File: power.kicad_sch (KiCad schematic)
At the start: 13 parts, among them J1 Conn_01x04, J2 Conn_01x04

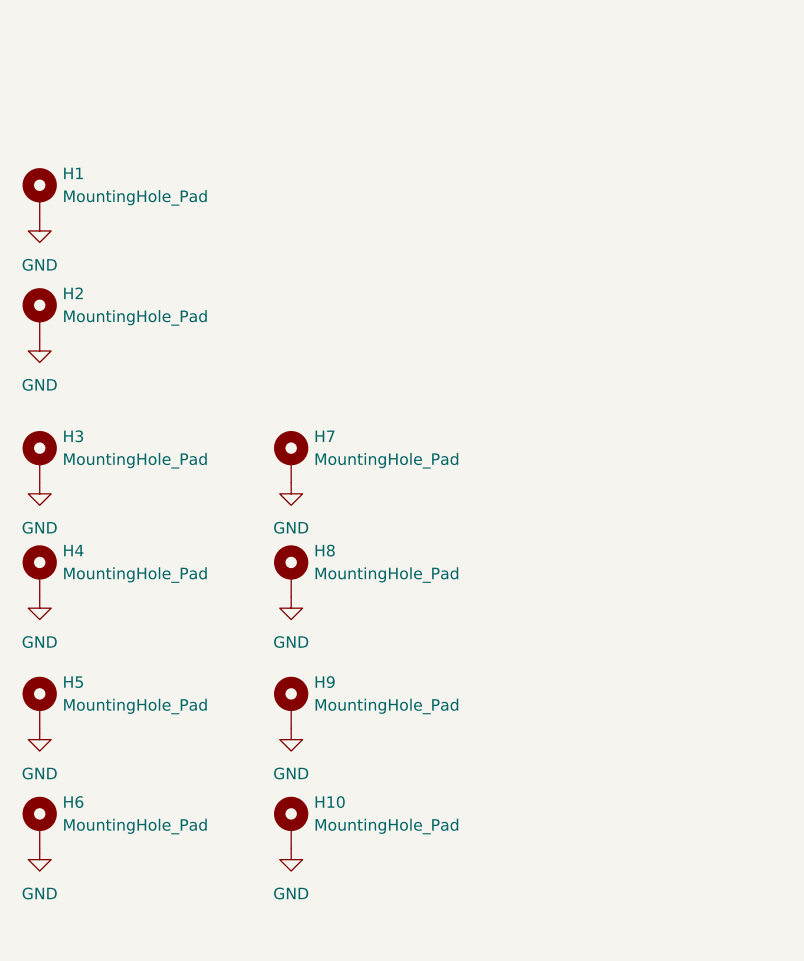
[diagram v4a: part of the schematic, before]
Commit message: correct hole positions
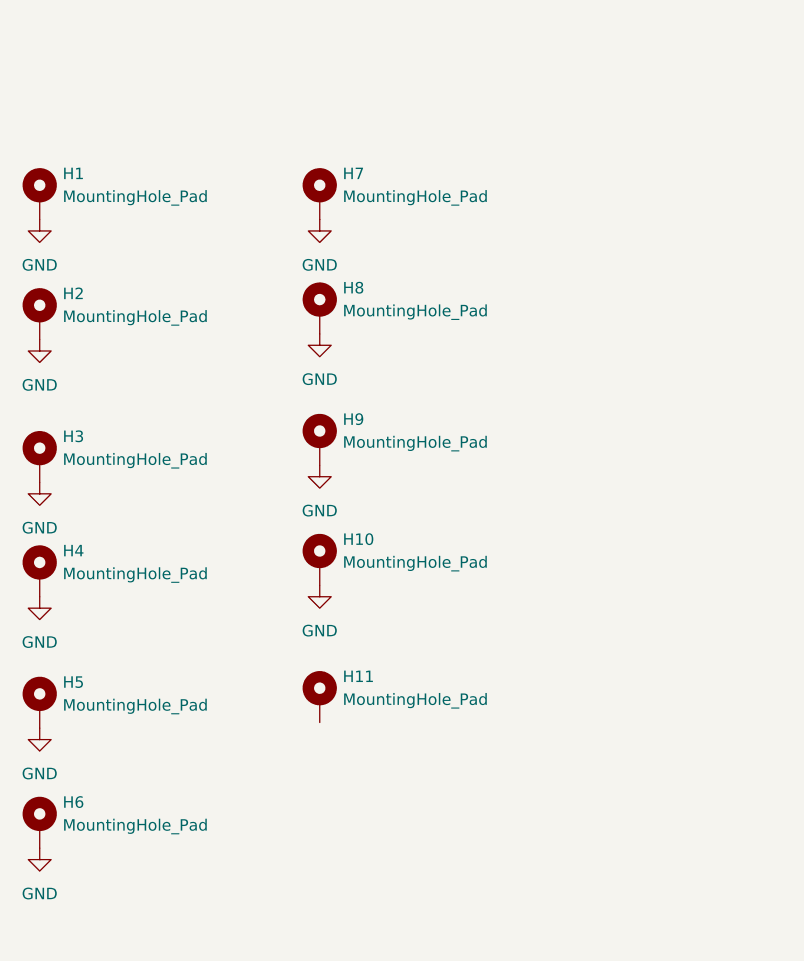
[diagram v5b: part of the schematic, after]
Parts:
- added H11: MountingHole_Pad, MountingHole:MountingHole_3.2mm_M3_DIN965_Pad, symbol Mechanical:MountingHole_Pad
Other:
- moved on the sheet: H10, H7, H8, H9
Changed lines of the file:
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@@
     )
   )
-  (symbol (lib_id "power:GND") (at 47.625 143.51 0) (unit 1)
-    (in_bom yes) (on_board yes) (fields_autoplaced)
-    (property "Reference" "#PWR07" (id 0) (at 47.625 149.86 0)
-      (effects (font (size 1.27 1.27)) hide)
-    )
-    (property "Value" "GND" (id 1) (at 47.625 148.59 0))
-    (property "Footprint" "" (id 2) (at 47.625 143.51 0)
-      (effects (font (size 1.27 1.27)) hide)
-    )
-    (property "Datasheet" "" (id 3) (at 47.625 143.51 0)
+  (symbol (lib_id "power:GND") (at 50.8 114.3 0) (unit 1)
+    (in_bom yes) (on_board yes) (fields_autoplaced)
+    (property "Reference" "#PWR07" (id 0) (at 50.8 120.65 0)
+      (effects (font (size 1.27 1.27)) hide)
+    )
+    (property "Value" "GND" (id 1) (at 50.8 119.38 0))
+    (property "Footprint" "" (id 2) (at 50.8 114.3 0)
+      (effects (font (size 1.27 1.27)) hide)
+    )
+    (property "Datasheet" "" (id 3) (at 50.8 114.3 0)
       (effects (font (size 1.27 1.27)) hide)
     )
@@
     (pin "1")
   )
-  (symbol (lib_id "Mechanical:MountingHole_Pad") (at 47.625 181.61 0) (unit 1)
-    (in_bom yes) (on_board yes) (fields_autoplaced)
-    (property "Reference" "H10" (id 0) (at 50.165 179.0699 0)
-      (effects (font (size 1.27 1.27)) (justify left))
-    )
-    (property "Value" "MountingHole_Pad" (id 1) (at 50.165 181.6099 0)
-      (effects (font (size 1.27 1.27)) (justify left))
-    )
-    (property "Footprint" "MountingHole:MountingHole_3.2mm_M3_DIN965_Pad" (id 2) (at 47.625 181.61 0)
-      (effects (font (size 1.27 1.27)) hide)
-    )
-    (property "Datasheet" "~" (id 3) (at 47.625 181.61 0)
+  (symbol (lib_id "Mechanical:MountingHole_Pad") (at 50.8 152.4 0) (unit 1)
+    (in_bom yes) (on_board yes)
+    (property "Reference" "H10" (id 0) (at 53.34 149.8599 0)
+      (effects (font (size 1.27 1.27)) (justify left))
+    )
+    (property "Value" "MountingHole_Pad" (id 1) (at 53.34 152.3999 0)
+      (effects (font (size 1.27 1.27)) (justify left))
+    )
+    (property "Footprint" "MountingHole:MountingHole_3.2mm_M3_DIN965_Pad" (id 2) (at 50.8 152.4 0)
+      (effects (font (size 1.27 1.27)) hide)
+    )
+    (property "Datasheet" "~" (id 3) (at 50.8 152.4 0)
       (effects (font (size 1.27 1.27)) hide)
     )
@@
     )
   )
-  (symbol (lib_id "Mechanical:MountingHole_Pad") (at 47.625 168.275 0) (unit 1)
-    (in_bom yes) (on_board yes) (fields_autoplaced)
-    (property "Reference" "H9" (id 0) (at 50.165 165.7349 0)
-      (effects (font (size 1.27 1.27)) (justify left))
-    )
-    (property "Value" "MountingHole_Pad" (id 1) (at 50.165 168.2749 0)
-      (effects (font (size 1.27 1.27)) (justify left))
-    )
-    (property "Footprint" "MountingHole:MountingHole_3.2mm_M3_DIN965_Pad" (id 2) (at 47.625 168.275 0)
-      (effects (font (size 1.27 1.27)) hide)
-    )
-    (property "Datasheet" "~" (id 3) (at 47.625 168.275 0)
+  (symbol (lib_id "Mechanical:MountingHole_Pad") (at 50.8 139.065 0) (unit 1)
+    (in_bom yes) (on_board yes)
+    (property "Reference" "H9" (id 0) (at 53.34 136.5249 0)
+      (effects (font (size 1.27 1.27)) (justify left))
+    )
+    (property "Value" "MountingHole_Pad" (id 1) (at 53.34 139.0649 0)
+      (effects (font (size 1.27 1.27)) (justify left))
+    )
+    (property "Footprint" "MountingHole:MountingHole_3.2mm_M3_DIN965_Pad" (id 2) (at 50.8 139.065 0)
+      (effects (font (size 1.27 1.27)) hide)
+    )
+    (property "Datasheet" "~" (id 3) (at 50.8 139.065 0)
       (effects (font (size 1.27 1.27)) hide)
     )
@@
     (pin "1")
   )
-  (symbol (lib_id "Mechanical:MountingHole_Pad") (at 47.625 153.67 0) (unit 1)
-    (in_bom yes) (on_board yes) (fields_autoplaced)
-    (property "Reference" "H8" (id 0) (at 50.165 151.1299 0)
-      (effects (font (size 1.27 1.27)) (justify left))
-    )
-    (property "Value" "MountingHole_Pad" (id 1) (at 50.165 153.6699 0)
-      (effects (font (size 1.27 1.27)) (justify left))
-    )
-    (property "Footprint" "MountingHole:MountingHole_3.2mm_M3_DIN965_Pad" (id 2) (at 47.625 153.67 0)
-      (effects (font (size 1.27 1.27)) hide)
-    )
-    (property "Datasheet" "~" (id 3) (at 47.625 153.67 0)
-      (effects (font (size 1.27 1.27)) hide)
-    )
-    (pin "1")
-  )
-  (symbol (lib_id "power:GND") (at 47.625 156.21 0) (unit 1)
-    (in_bom yes) (on_board yes) (fields_autoplaced)
-    (property "Reference" "#PWR08" (id 0) (at 47.625 162.56 0)
-      (effects (font (size 1.27 1.27)) hide)
-    )
-    (property "Value" "GND" (id 1) (at 47.625 161.29 0))
-    (property "Footprint" "" (id 2) (at 47.625 156.21 0)
-      (effects (font (size 1.27 1.27)) hide)
-    )
-    (property "Datasheet" "" (id 3) (at 47.625 156.21 0)
-      (effects (font (size 1.27 1.27)) hide)
-    )
-    (pin "1")
-  )
-  (symbol (lib_id "power:GND") (at 47.625 170.815 0) (unit 1)
-    (in_bom yes) (on_board yes) (fields_autoplaced)
-    (property "Reference" "#PWR09" (id 0) (at 47.625 177.165 0)
-      (effects (font (size 1.27 1.27)) hide)
-    )
-    (property "Value" "GND" (id 1) (at 47.625 175.895 0))
-    (property "Footprint" "" (id 2) (at 47.625 170.815 0)
-      (effects (font (size 1.27 1.27)) hide)
-    )
-    (property "Datasheet" "" (id 3) (at 47.625 170.815 0)
+  (symbol (lib_id "Mechanical:MountingHole_Pad") (at 50.8 124.46 0) (unit 1)
+    (in_bom yes) (on_board yes)
+    (property "Reference" "H8" (id 0) (at 53.34 121.9199 0)
+      (effects (font (size 1.27 1.27)) (justify left))
+    )
+    (property "Value" "MountingHole_Pad" (id 1) (at 53.34 124.4599 0)
+      (effects (font (size 1.27 1.27)) (justify left))
+    )
+    (property "Footprint" "MountingHole:MountingHole_3.2mm_M3_DIN965_Pad" (id 2) (at 50.8 124.46 0)
+      (effects (font (size 1.27 1.27)) hide)
+    )
+    (property "Datasheet" "~" (id 3) (at 50.8 124.46 0)
+      (effects (font (size 1.27 1.27)) hide)
+    )
+    (pin "1")
+  )
+  (symbol (lib_id "power:GND") (at 50.8 127 0) (unit 1)
+    (in_bom yes) (on_board yes) (fields_autoplaced)
+    (property "Reference" "#PWR08" (id 0) (at 50.8 133.35 0)
+      (effects (font (size 1.27 1.27)) hide)
+    )
+    (property "Value" "GND" (id 1) (at 50.8 132.08 0))
+    (property "Footprint" "" (id 2) (at 50.8 127 0)
+      (effects (font (size 1.27 1.27)) hide)
+    )
+    (property "Datasheet" "" (id 3) (at 50.8 127 0)
+      (effects (font (size 1.27 1.27)) hide)
+    )
+    (pin "1")
+  )
+  (symbol (lib_id "power:GND") (at 50.8 141.605 0) (unit 1)
+    (in_bom yes) (on_board yes) (fields_autoplaced)
+    (property "Reference" "#PWR09" (id 0) (at 50.8 147.955 0)
+      (effects (font (size 1.27 1.27)) hide)
+    )
+    (property "Value" "GND" (id 1) (at 50.8 146.685 0))
+    (property "Footprint" "" (id 2) (at 50.8 141.605 0)
+      (effects (font (size 1.27 1.27)) hide)
+    )
+    (property "Datasheet" "" (id 3) (at 50.8 141.605 0)
       (effects (font (size 1.27 1.27)) hide)
     )
@@
     (pin "1")
   )
-  (symbol (lib_id "power:GND") (at 47.625 184.15 0) (unit 1)
-    (in_bom yes) (on_board yes) (fields_autoplaced)
-    (property "Reference" "#PWR010" (id 0) (at 47.625 190.5 0)
-      (effects (font (size 1.27 1.27)) hide)
-    )
-    (property "Value" "GND" (id 1) (at 47.625 189.23 0))
-    (property "Footprint" "" (id 2) (at 47.625 184.15 0)
-      (effects (font (size 1.27 1.27)) hide)
-    )
-    (property "Datasheet" "" (id 3) (at 47.625 184.15 0)
+  (symbol (lib_id "power:GND") (at 50.8 154.94 0) (unit 1)
+    (in_bom yes) (on_board yes) (fields_autoplaced)
+    (property "Reference" "#PWR010" (id 0) (at 50.8 161.29 0)
+      (effects (font (size 1.27 1.27)) hide)
+    )
+    (property "Value" "GND" (id 1) (at 50.8 160.02 0))
+    (property "Footprint" "" (id 2) (at 50.8 154.94 0)
+      (effects (font (size 1.27 1.27)) hide)
+    )
+    (property "Datasheet" "" (id 3) (at 50.8 154.94 0)
       (effects (font (size 1.27 1.27)) hide)
     )
@@
     (pin "1")
   )
+  (symbol (lib_id "Mechanical:MountingHole_Pad") (at 50.8 167.64 0) (unit 1)
+    (in_bom yes) (on_board yes)
+    (property "Reference" "H11" (id 0) (at 53.34 165.0999 0)
+      (effects (font (size 1.27 1.27)) (justify left))
+    )
+    (property "Value" "MountingHole_Pad" (id 1) (at 53.34 167.6399 0)
+      (effects (font (size 1.27 1.27)) (justify left))
+    )
+    (property "Footprint" "MountingHole:MountingHole_3.2mm_M3_DIN965_Pad" (id 2) (at 50.8 167.64 0)
+      (effects (font (size 1.27 1.27)) hide)
+    )
+    (property "Datasheet" "~" (id 3) (at 50.8 167.64 0)
+      (effects (font (size 1.27 1.27)) hide)
+    )
+    (pin "1")
+  )
   (symbol (lib_id "power:+5V") (at 133.35 86.36 0) (unit 1)
     (in_bom yes) (on_board yes) (fields_autoplaced)
@@
     (pin "1")
   )
-  (symbol (lib_id "Mechanical:MountingHole_Pad") (at 47.625 140.97 0) (unit 1)
-    (in_bom yes) (on_board yes) (fields_autoplaced)
-    (property "Reference" "H7" (id 0) (at 50.165 138.4299 0)
-      (effects (font (size 1.27 1.27)) (justify left))
-    )
-    (property "Value" "MountingHole_Pad" (id 1) (at 50.165 140.9699 0)
-      (effects (font (size 1.27 1.27)) (justify left))
-    )
-    (property "Footprint" "MountingHole:MountingHole_3.2mm_M3_DIN965_Pad" (id 2) (at 47.625 140.97 0)
-      (effects (font (size 1.27 1.27)) hide)
-    )
-    (property "Datasheet" "~" (id 3) (at 47.625 140.97 0)
-      (effects (font (size 1.27 1.27)) hide)
-    )
+  (symbol (lib_id "Mechanical:MountingHole_Pad") (at 50.8 111.76 0) (unit 1)
+    (in_bom yes) (on_board yes)
+    (property "Reference" "H7" (id 0) (at 53.34 109.2199 0)
+      (effects (font (size 1.27 1.27)) (justify left))
+    )
+    (property "Value" "MountingHole_Pad" (id 1) (at 53.34 111.7599 0)
+      (effects (font (size 1.27 1.27)) (justify left))
+    )
+    (property "Footprint" "MountingHole:MountingHole_3.2mm_M3_DIN965_Pad" (id 2) (at 50.8 111.76 0)
+      (effects (font (size 1.27 1.27)) hide)
+    )
+    (property "Datasheet" "~" (id 3) (at 50.8 111.76 0)
+      (effects (font (size 1.27 1.27)) hide)
+    )
